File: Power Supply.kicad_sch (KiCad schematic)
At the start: 46 parts, among them CN1 26-60-4120, CN10 26-60-4030, CN2 26-60-4060, CN3 26-60-4100, CN4 26-60-4120, CN5 26-60-4080, CN6 26-60-4150, CN7 26-60-4050, CN8 26-60-4090, CN9 26-60-4040

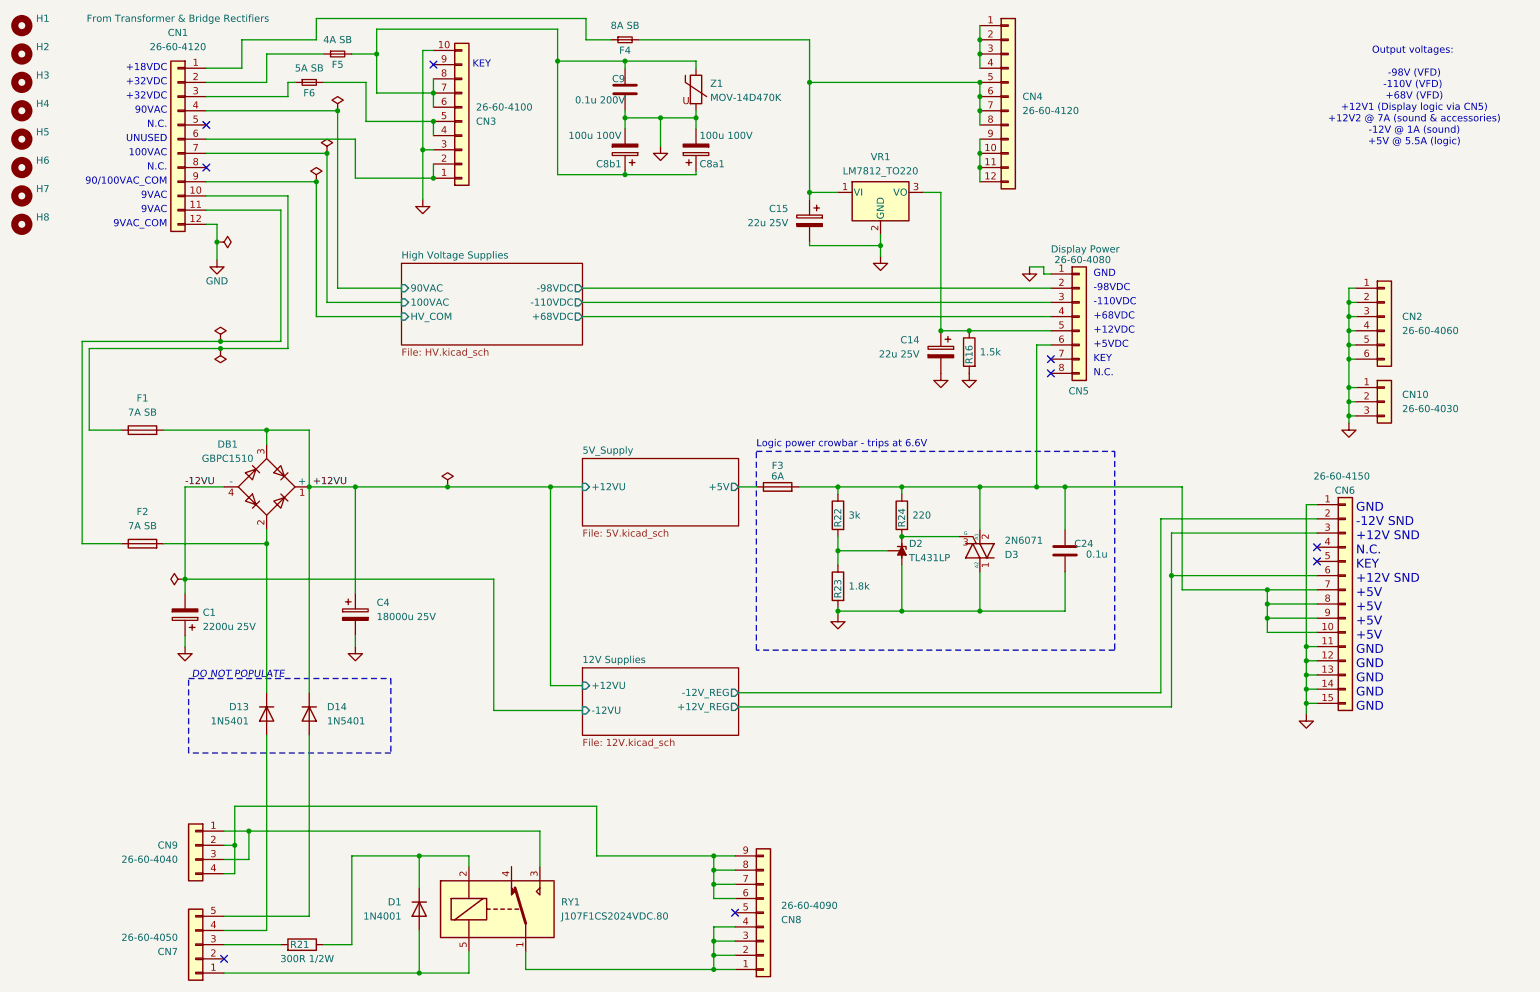
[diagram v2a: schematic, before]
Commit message: Finished schematic; began placing and routing board. 12V regulation section still not placed, and HV section not routed.
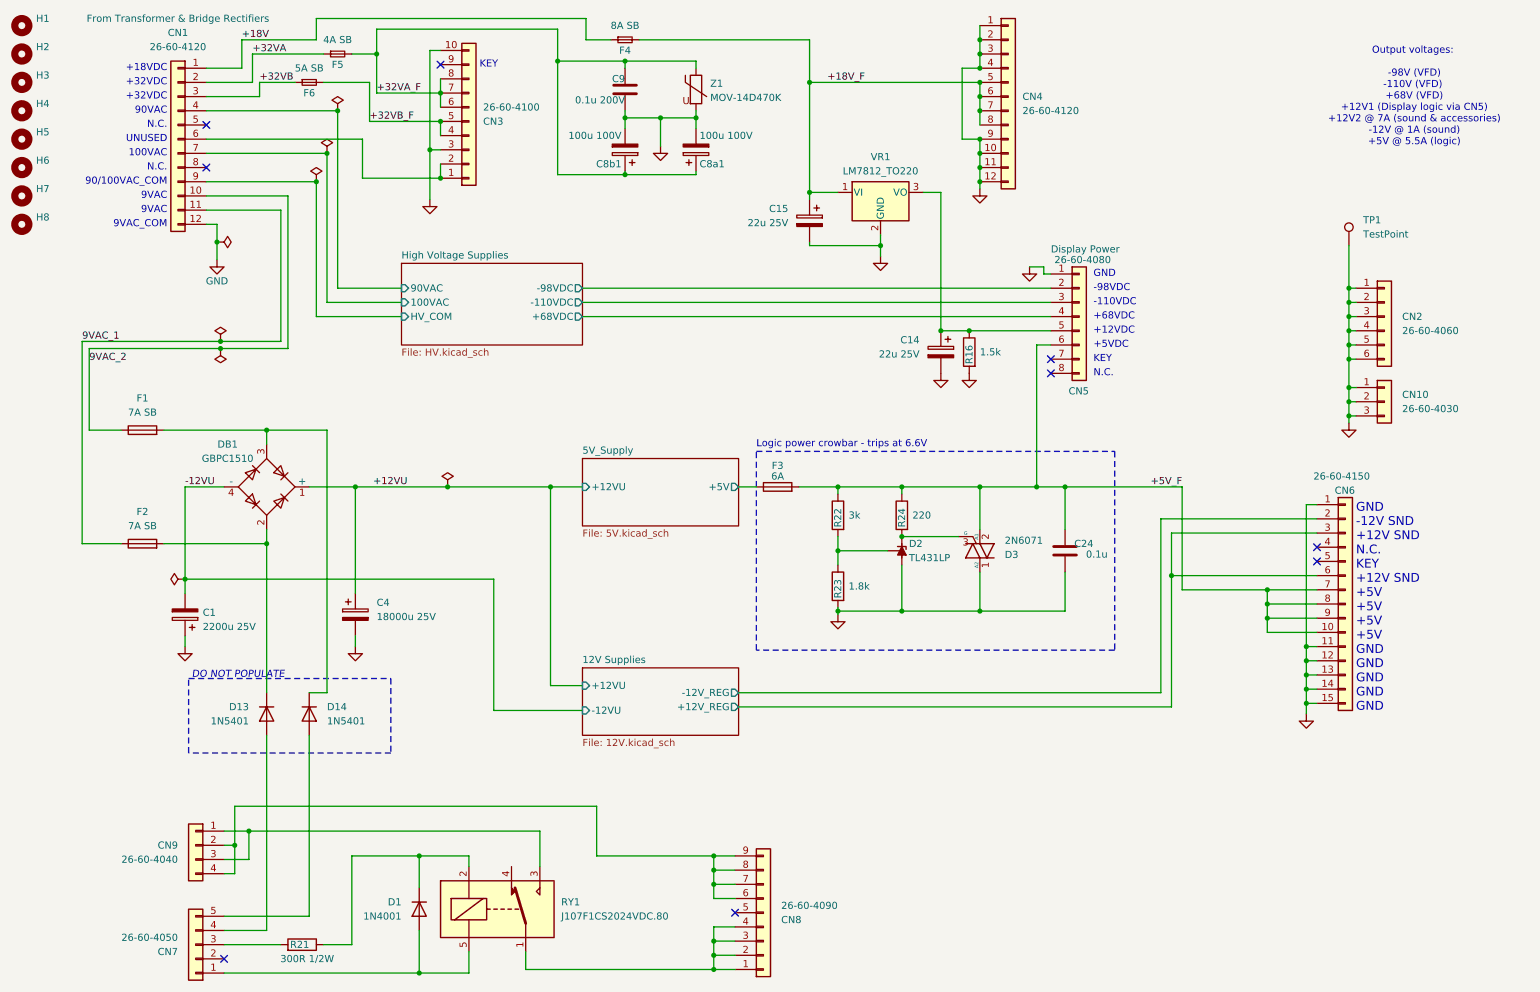
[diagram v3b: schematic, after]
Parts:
- added TP1: TestPoint, TestPoint:TestPoint_Loop_D2.60mm_Drill1.4mm_Beaded, symbol Connector:TestPoint
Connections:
- net +12VU: no longer D14.1 (K), DB1.3, F1.2
- net GND: now also CN4.1 (Pin_1), CN4.10 (Pin_10), CN4.11 (Pin_11), CN4.12 (Pin_12), CN4.2 (Pin_2), CN4.3 (Pin_3), CN4.4 (Pin_4), CN4.9 (Pin_9), TP1.1
- net +32VA_F: now reaches C8a1.1, C8b1.1, C9.1, CN3.6 (Pin_6), CN3.7 (Pin_7), CN3.8 (Pin_8), F5.2, Z1.1
- net +18V_F: now reaches C15.1, CN4.5 (Pin_5), CN4.6 (Pin_6), CN4.7 (Pin_7), CN4.8 (Pin_8), F4.2, VR1.1 (VI)
- net +5V_F: now reaches C24.2, CN5.6 (Pin_6), CN6.10 (Pin_10), CN6.7 (Pin_7), CN6.8 (Pin_8), CN6.9 (Pin_9), D3.2 (A1), F3.2, R22.1, R24.1
- net +32VA: now reaches CN1.2 (Pin_2), F5.1
- net +18V: now reaches CN1.1 (Pin_1), F4.1
- net 9VAC_2: now reaches CN1.10 (Pin_10), F1.1
- net 9VAC_1: now reaches CN1.11 (Pin_11), F2.1
- net +32VB: now reaches CN1.3 (Pin_3), F6.1
- net +32VB_F: now reaches CN3.4 (Pin_4), CN3.5 (Pin_5), F6.2
- new net: D14.1 (K), DB1.3, F1.2
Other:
- moved on the sheet: CN3

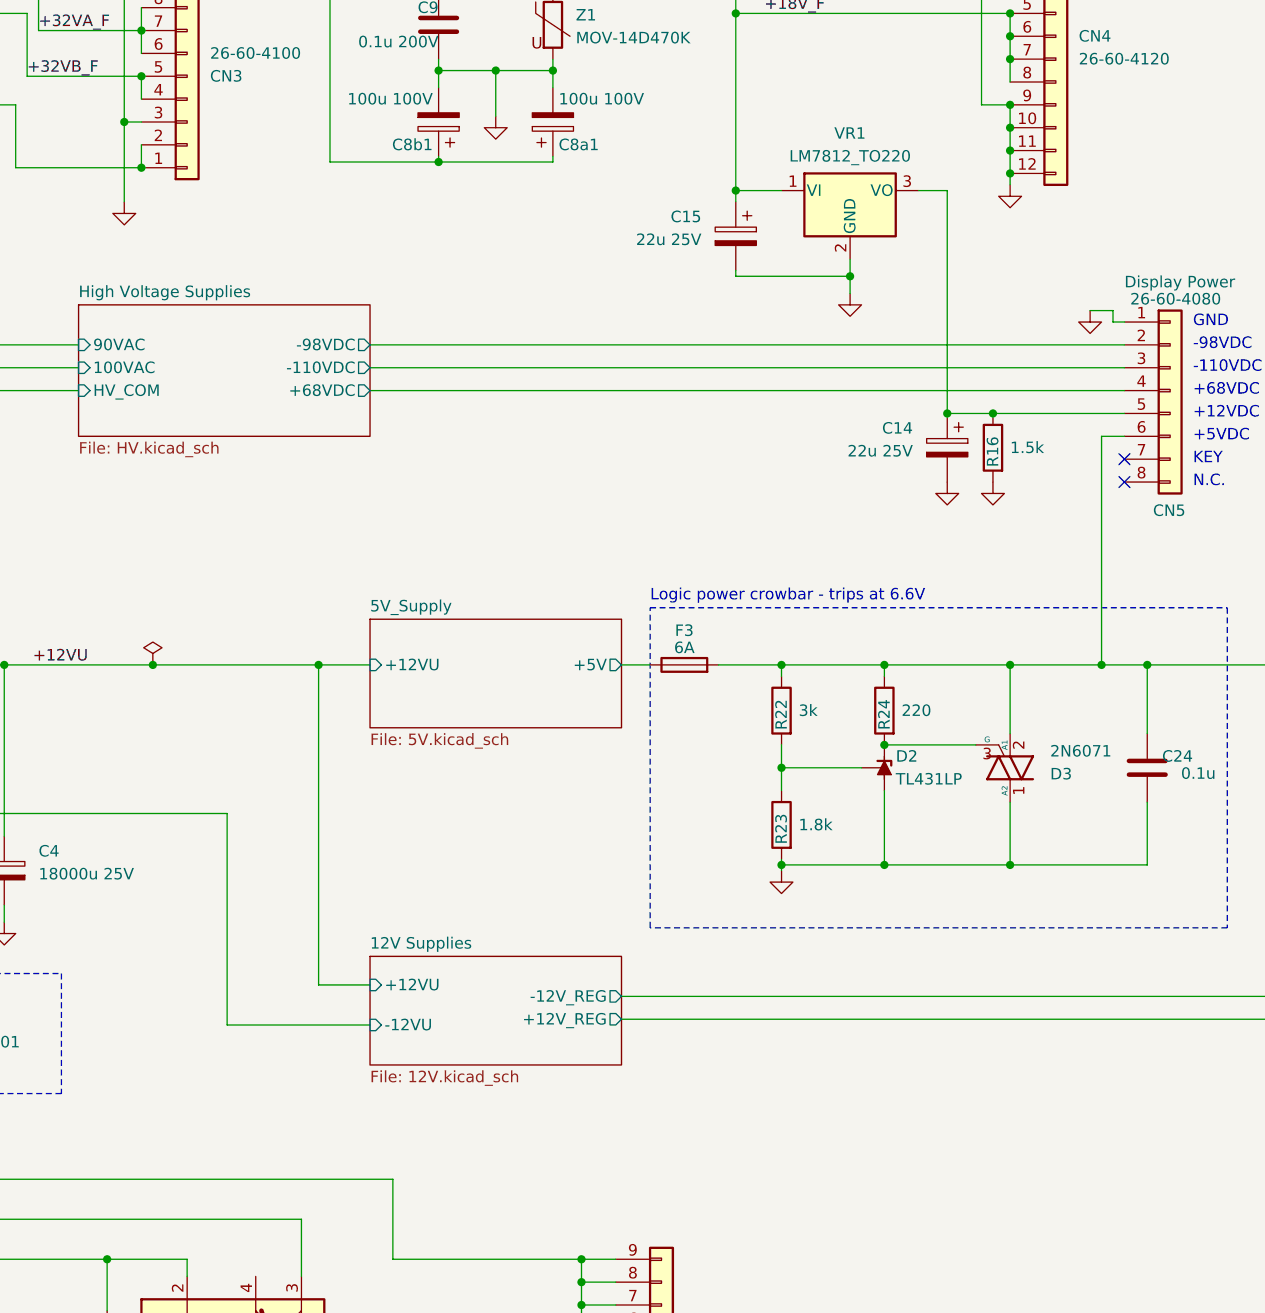
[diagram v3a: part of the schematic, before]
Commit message: Finished routing. While DRC fails with some errors, some can be disregarded. Need to do some cleanups to get rid of the others.
Also, added 3 discharge resistors to the schematic.
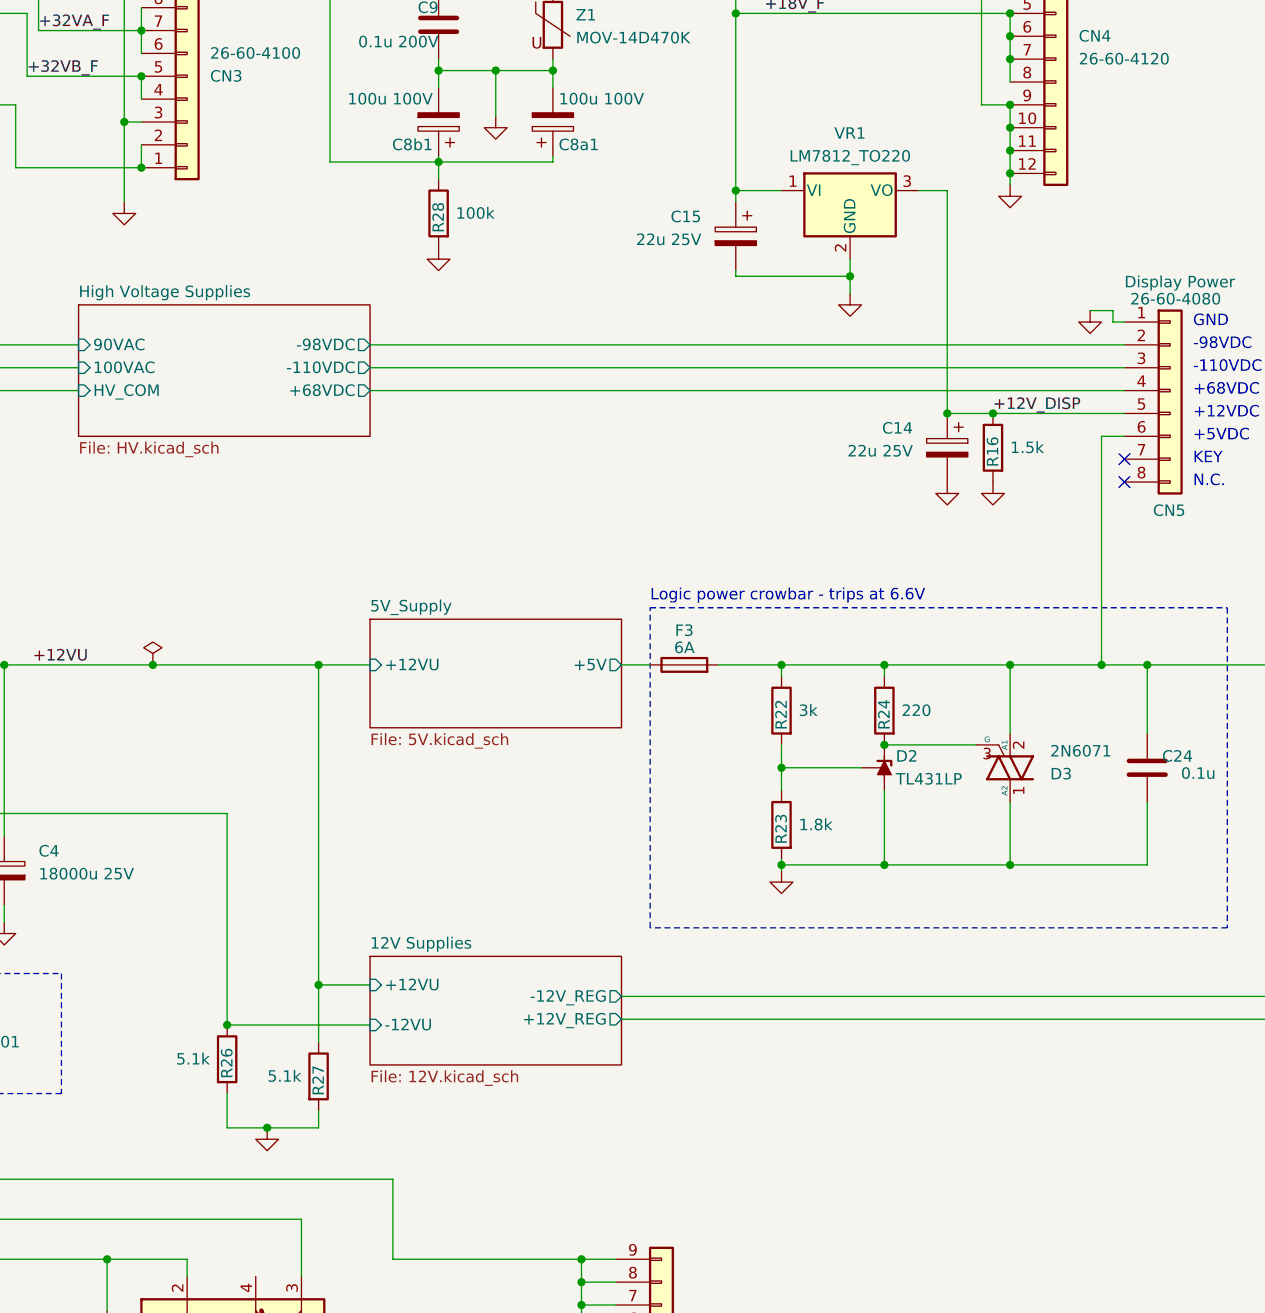
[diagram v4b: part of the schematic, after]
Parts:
- added R26, R27: 5.1k, Resistor_THT:R_Axial_DIN0309_L9.0mm_D3.2mm_P15.24mm_Horizontal, symbol Device:R
- added R28: 100k, Resistor_THT:R_Axial_DIN0309_L9.0mm_D3.2mm_P15.24mm_Horizontal, symbol Device:R
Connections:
- net +12VU: now also R27.1
- net +32VA_F: now also R28.1
- net -12VU: now also R26.1
- net GND: now also R26.2, R27.2, R28.2
- net +12V_DISP: now reaches C14.1, CN5.5 (Pin_5), R16.1, VR1.3 (VO)

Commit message: Final version, though yet untested.
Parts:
- C9: footprint Capacitor_THT:C_Rect_L4.6mm_W3.0mm_P2.50mm_MKS02_FKP02 -> Capacitor_THT:C_Rect_L7.0mm_W3.5mm_P2.50mm_P5.00mm
- D13, D14: now not fitted
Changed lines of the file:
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@@
 			)
 		)
-		(property "Footprint" "Capacitor_THT:C_Rect_L4.6mm_W3.0mm_P2.50mm_MKS02_FKP02"
+		(property "Footprint" "Capacitor_THT:C_Rect_L7.0mm_W3.5mm_P2.50mm_P5.00mm"
 			(at 124.1552 30.48 0)
 			(effects
@@
 		(in_bom yes)
 		(on_board yes)
-		(dnp no)
+		(dnp yes)
 		(property "Reference" "D13"
 			(at 55.88 137.1599 90)
@@
 		(in_bom yes)
 		(on_board yes)
-		(dnp no)
+		(dnp yes)
 		(property "Reference" "D14"
 			(at 69.85 137.1599 90)

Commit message: Changed TO-92 packages to non-inlined versions for easier soldering Fixed issue with HV section input voltage; the original schematics are wrong in that the power should come exclusively from the 100V (or 90V) AC supply, and not one from each for positive/negative. Increased the drill sizes of some packages to better fit larger wires from devices in BOM. Assigned an unused pin on CN1 to use as a key, so it cannot be cross-plugged with CN4.
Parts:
- D2: footprint Package_TO_SOT_THT:TO-92_Inline -> Package_TO_SOT_THT:TO-92
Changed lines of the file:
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@@
 			)
 		)
-		(property "Footprint" "Package_TO_SOT_THT:TO-92_Inline"
+		(property "Footprint" "Package_TO_SOT_THT:TO-92"
 			(at 177.546 109.22 0)
 			(effects
